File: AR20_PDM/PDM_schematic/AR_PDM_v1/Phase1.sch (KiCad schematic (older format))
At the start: 22 parts, among them Q1 BTS50025-1TAD, U1 INA233

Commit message: Added LEDs and switches.
- Added all status leds
- Added all switches
- ! Connections are work in progress, not everything is correct
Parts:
- removed D?: P1_Active, symbol Device:LED
- removed R? (x2): 4k7, symbol AR20_PDM_v1-rescue:R-Device
- removed R?: RLED, symbol AR20_PDM_v1-rescue:R-Device
- removed U? (x2): Fet-P, symbol AR20_PDM_v1-rescue:GenericFet-P
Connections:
- net labels added: P1_MOS_IN
- net labels removed: P1_Alert, P1_EN_ACM, P1_EN_AUX
- wire segments 81 -> 59
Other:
- note removed: "Use Logic Level Mosfets. (Gs Threshold <3.3V)\nP-mos array might be used"
- moved on the sheet: C_sense?

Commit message: Fixed wrong value components and ports, wiring, see discription
- Fixed supply cappacitor value 220 nf to 100nf
- Fixed IN cappacitor value 220 nf to 150 nf
- Fixed out cappacitor value, 220nf to 10 nf
- Made a mux for mosfet sense
- Found a I/O port expander
- Added some and removed some leds
- Fixed all labels, and wired everything up, besides the connectors
- Still missing connector and acm connector pinout.
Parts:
- removed C_sense?: 0.1uf, symbol AR20_PDM_v1-rescue:C-Device
- C_bypass: value 0.1uF -> 100nf
- C_in: value 220nf -> 150nf
- C_out: value 220nf -> 10nf
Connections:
- wire segments 59 -> 57
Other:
- note removed: "Ceramic, Place close to respective phase, mosfet/relay"
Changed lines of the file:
@@
 $Descr A4 11693 8268
 encoding utf-8
-Sheet 4 11
+Sheet 4 13
 Title ""
 Date ""
@@
 AR Path="/5E10174B/5DAAC1D1" Ref="C_out?"  Part="1"
 F 0 "C_out" H 4915 2896 50  0000 L CNN
-F 1 "220nf" H 4915 2805 50  0000 L CNN
+F 1 "10nf" H 4915 2805 50  0000 L CNN
 F 2 "" H 4838 2700 50  0001 C CNN
 F 3 "~" H 4800 2850 50  0001 C CNN
@@
 AR Path="/5E10174B/5DAAC1D7" Ref="C_in?"  Part="1"
 F 0 "C_in" H 3615 1996 50  0000 L CNN
-F 1 "220nf" H 3615 1905 50  0000 L CNN
+F 1 "150nf" H 3615 1905 50  0000 L CNN
 F 2 "" H 3538 1800 50  0001 C CNN
 F 3 "~" H 3500 1950 50  0001 C CNN
@@
 AR Path="/5E10174B/5DAAC201" Ref="C_bypass?"  Part="1"
 F 0 "C_bypass" V 8248 3350 50  0000 C CNN
-F 1 "0.1uF" V 8339 3350 50  0000 C CNN
+F 1 "100nf" V 8339 3350 50  0000 C CNN
 F 2 "" H 8538 3200 50  0001 C CNN
 F 3 "~" H 8500 3350 50  0001 C CNN
@@
 Wire Wire Line
 	6575 4300 8750 4300
-$Comp
-L AR20_PDM_v1-rescue:C-Device C_sense?
-U 1 1 5E10B301
-P 7225 1925
-AR Path="/5DA89415/5E10B301" Ref="C_sense?"  Part="1"
-AR Path="/5DEB10A1/5E10B301" Ref="C_sense?"  Part="1"
-AR Path="/5DEB20EA/5E10B301" Ref="C_sense?"  Part="1"
-AR Path="/5E0E4725/5E10B301" Ref="C_sense?"  Part="1"
-AR Path="/5E0E4A93/5E10B301" Ref="C_sense?"  Part="1"
-AR Path="/5E0E4EB5/5E10B301" Ref="C_sense?"  Part="1"
-AR Path="/5E0E5304/5E10B301" Ref="C_sense?"  Part="1"
-AR Path="/5E0E594B/5E10B301" Ref="C_sense?"  Part="1"
-AR Path="/5E0E607C/5E10B301" Ref="C_sense?"  Part="1"
-AR Path="/5E0FB5C8/5E10B301" Ref="C_sense?"  Part="1"
-AR Path="/5E0FBBBD/5E10B301" Ref="C_sense?"  Part="1"
-AR Path="/5E0FC3A2/5E10B301" Ref="C_sense?"  Part="1"
-AR Path="/5E0FCFDC/5E10B301" Ref="C_sense?"  Part="1"
-AR Path="/5E0FDCCC/5E10B301" Ref="C_sense?"  Part="1"
-AR Path="/5E10174B/5E10B301" Ref="C_sense?"  Part="1"
-F 0 "C_sense?" H 7340 1971 50  0000 L CNN
-F 1 "0.1uf" H 7340 1880 50  0000 L CNN
-F 2 "" H 7263 1775 50  0001 C CNN
-F 3 "~" H 7225 1925 50  0001 C CNN
-	1    7225 1925
-	-1   0    0    1
-$EndComp
-$Comp
-L AR20_PDM_v1-rescue:GND-power #PWR?
-U 1 1 5E1293CC
-P 7225 2075
-AR Path="/5DA89415/5E1293CC" Ref="#PWR?"  Part="1"
-AR Path="/5DEB10A1/5E1293CC" Ref="#PWR?"  Part="1"
-AR Path="/5DEB20EA/5E1293CC" Ref="#PWR?"  Part="1"
-AR Path="/5E0E4725/5E1293CC" Ref="#PWR?"  Part="1"
-AR Path="/5E0E4A93/5E1293CC" Ref="#PWR?"  Part="1"
-AR Path="/5E0E4EB5/5E1293CC" Ref="#PWR?"  Part="1"
-AR Path="/5E0E5304/5E1293CC" Ref="#PWR?"  Part="1"
-AR Path="/5E0E594B/5E1293CC" Ref="#PWR?"  Part="1"
-AR Path="/5E0E607C/5E1293CC" Ref="#PWR?"  Part="1"
-AR Path="/5E0FB5C8/5E1293CC" Ref="#PWR?"  Part="1"
-AR Path="/5E0FBBBD/5E1293CC" Ref="#PWR?"  Part="1"
-AR Path="/5E0FC3A2/5E1293CC" Ref="#PWR?"  Part="1"
-AR Path="/5E0FCFDC/5E1293CC" Ref="#PWR?"  Part="1"
-AR Path="/5E0FDCCC/5E1293CC" Ref="#PWR?"  Part="1"
-AR Path="/5E10174B/5E1293CC" Ref="#PWR?"  Part="1"
-F 0 "#PWR?" H 7225 1825 50  0001 C CNN
-F 1 "GND" H 7230 1902 50  0000 C CNN
-F 2 "" H 7225 2075 50  0001 C CNN
-F 3 "" H 7225 2075 50  0001 C CNN
-	1    7225 2075
-	1    0    0    -1
-$EndComp
-Wire Wire Line
-	7225 1775 7225 1675
-Wire Wire Line
-	7225 1675 7150 1675
-Text Notes 6800 2400 0    50   ~ 0
-Ceramic, Place close to respective phase, mosfet/relay
 Wire Wire Line
 	3700 3225 4525 3225
@@
 Text HLabel 4650 1600 0    50   Input ~ 10
 V+12V
-Text HLabel 7150 1675 0    50   Input ~ 10
-V+12V
-Wire Notes Line
-	6725 1600 9050 1600
-Wire Notes Line
-	9050 1600 9050 2450
-Wire Notes Line
-	9050 2450 6725 2450
-Wire Notes Line
-	6725 2450 6725 1600
 Wire Wire Line
 	2250 2400 3150 2400

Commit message: Fixed issues, controlled components, BOM, see discription
- added acm symbol
- fixed wrongly faced P-mosfets
- I/O expander now sinks led instead of source
- Bill of material mostly done
- Correct address for INA233 chips.
- Now 4 diodes serves as flyback for all mosfets
- Corrected naming scheme for compmonents (everything is not fixed yet)
- Fixed some labels
- altso some minor changes
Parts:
- removed C_bypass, C_vs: 100nf, symbol AR20_PDM_v1-rescue:C-Device
- removed C_out, C_sense: 10nf, symbol AR20_PDM_v1-rescue:C-Device
- removed Cs?: 4.7uF, symbol AR20_PDM_v1-rescue:C-Device
- removed D?: 3.3-5V 5W, symbol AR20_PDM_v1-rescue:D_Zener-Device
- removed D?: 16V 5W, symbol AR20_PDM_v1-rescue:D_Zener-Device
- removed Q1: BTS50025-1TAD, symbol AR20_PDM_v1-rescue:BTS50025-1TAD
- removed R?: 4k7, symbol AR20_PDM_v1-rescue:R-Device
- removed R_Shunt: 5m_0.1%_30+A, symbol AR20_PDM_v1-rescue:R_Shunt-Device
- removed R_in: 4.7K, symbol AR20_PDM_v1-rescue:R-Device
- removed R_s?: 3.9R, symbol AR20_PDM_v1-rescue:R-Device
- removed R_sense: 1k, symbol AR20_PDM_v1-rescue:R-Device
- removed U1: INA233, symbol AR20_PDM_v1-rescue:INA233
- added C10: 4.7uF, Capacitor_SMD:C_1206_3216Metric, symbol AR20_PDM_v1-rescue:C-Device
- added C11, C9: 100nf, Capacitor_SMD:C_0603_1608Metric, symbol AR20_PDM_v1-rescue:C-Device
- added C6, C8: 10nf, Capacitor_SMD:C_0603_1608Metric, symbol AR20_PDM_v1-rescue:C-Device
- added Q3: BTS50025-1TAD, symbol AR20_PDM_v1-rescue:BTS50025-1TAD
- added R3, R4: 4k7, symbol AR20_PDM_v1-rescue:R-Device
- added R5: 1k, symbol AR20_PDM_v1-rescue:R-Device
- added R6: 3.9R, symbol AR20_PDM_v1-rescue:R-Device
- added R_Shunt4: 2m_1%_4W, symbol AR20_PDM_v1-rescue:R-Device
- added U5: INA233, symbol AR20_PDM_v1-rescue:INA233
- C7: renamed from C_in; footprint (none) -> Capacitor_SMD:C_0603_1608Metric
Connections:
- wire segments 57 -> 55
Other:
- note added: "addr: 1000000"

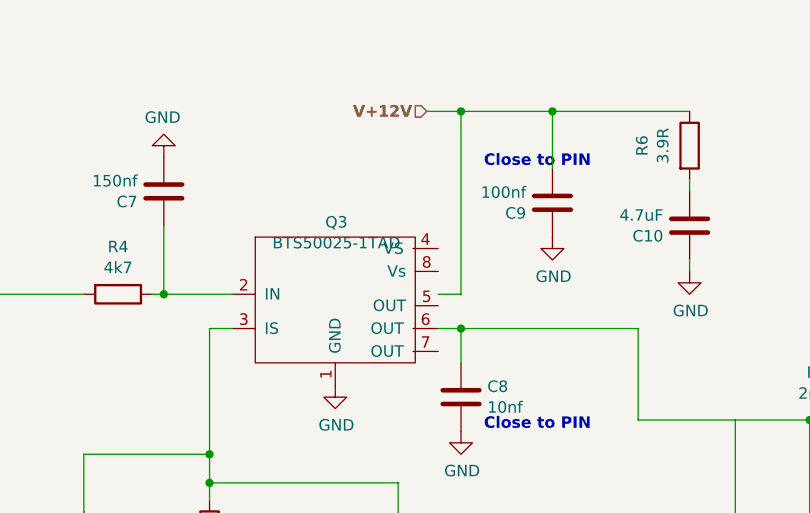
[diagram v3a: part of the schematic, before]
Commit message: PCB design, and issue fixing, work in progress
- Error fixed: Mux mosfet resistor change to ground
- Open drain output added on phase 6, for engine blipping purpose
- Most of pcb symbols and footprints are finished, including main connector
- PCB is change from 1oz to 2oz copper layer, for easier routing.
- Basic Draft of pcb is done, for now.
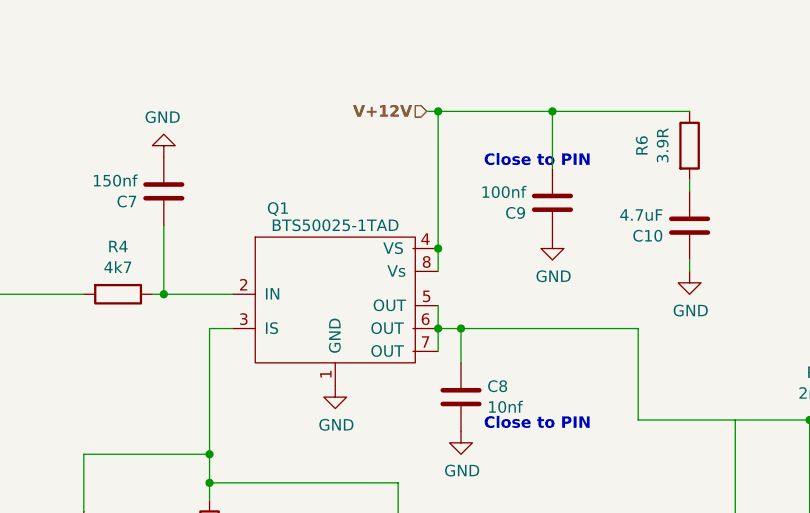
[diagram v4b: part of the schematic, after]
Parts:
- Q1: renamed from Q3; footprint (none) -> AR_PDM_v1:BTS500xx
- R3, R4, R5, R6: footprint (none) -> Resistor_SMD:R_0603_1608Metric
- R_Shunt4: footprint (none) -> Resistor_SMD:R_2512_6332Metric
- U5: footprint (none) -> AR_PDM_v1:INA233
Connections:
- net V+12V: now also Q1.4 (VS), Q1.8 (Vs)
- net at C8.1, Q1.6 (OUT), R_Shunt4.2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: now also Q1.5 (OUT), Q1.7 (OUT)
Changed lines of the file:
@@
 F 0 "R4" V 3093 2400 50  0000 C CNN
 F 1 "4k7" V 3184 2400 50  0000 C CNN
-F 2 "" V 3230 2400 50  0001 C CNN
+F 2 "Resistor_SMD:R_0603_1608Metric" V 3230 2400 50  0001 C CNN
 F 3 "~" H 3300 2400 50  0001 C CNN
 	1    3300 2400
@@
 F 0 "R3" H 2320 1896 50  0000 L CNN
 F 1 "4k7" H 2320 1805 50  0000 L CNN
-F 2 "" V 2180 1850 50  0001 C CNN
+F 2 "Resistor_SMD:R_0603_1608Metric" V 2180 1850 50  0001 C CNN
 F 3 "~" H 2250 1850 50  0001 C CNN
 	1    2250 1850
@@
 Wire Wire Line
 	3500 2100 3500 2400
-Connection ~ 3500 2400
-Wire Wire Line
-	3500 2400 3800 2400
-$Comp
-L AR20_PDM_v1-rescue:BTS50025-1TAD Q3
+$Comp
+L AR20_PDM_v1-rescue:BTS50025-1TAD Q1
 U 1 1 5E21B7FE
 P 4250 2650
-AR Path="/5DA89415/5E21B7FE" Ref="Q3"  Part="1"
+AR Path="/5DA89415/5E21B7FE" Ref="Q1"  Part="1"
 AR Path="/5DEB10A1/5E21B7FE" Ref="Q?"  Part="1"
 AR Path="/5DEB20EA/5E21B7FE" Ref="Q?"  Part="1"
@@
 AR Path="/5E0FDCCC/5E21B7FE" Ref="Q?"  Part="1"
 AR Path="/5E10174B/5E21B7FE" Ref="Q?"  Part="1"
-F 0 "Q3" H 4255 3215 50  0000 C CNN
-F 1 "BTS50025-1TAD" H 4255 3124 50  0000 C CNN
-F 2 "" H 4250 2650 50  0001 C CNN
+F 0 "Q1" H 4000 3275 50  0000 C CNN
+F 1 "BTS50025-1TAD" H 4250 3200 50  0000 C CNN
+F 2 "AR_PDM_v1:BTS500xx" H 4250 2650 50  0001 C CNN
 F 3 "" H 4250 2650 50  0001 C CNN
 	1    4250 2650
@@
 F 0 "U5" H 9225 4465 50  0000 C CNN
 F 1 "INA233" H 9225 4374 50  0000 C CNN
-F 2 "" H 9200 4050 50  0001 C CNN
+F 2 "AR_PDM_v1:INA233" H 9200 4050 50  0001 C CNN
 F 3 "" H 9200 4050 50  0001 C CNN
 	1    9200 4050
@@
 Wire Wire Line
 	3700 3100 3700 3225
-Wire Wire Line
-	4700 2400 4800 2400
-Wire Wire Line
-	4800 2400 4800 1600
-Wire Wire Line
-	4800 1600 4650 1600
 Text HLabel 2250 1550 1    50   Input ~ 10
 vcc_5v
@@
 F 0 "R6" V 5593 1750 50  0000 C CNN
 F 1 "3.9R" V 5684 1750 50  0000 C CNN
-F 2 "" V 5730 1750 50  0001 C CNN
+F 2 "Resistor_SMD:R_0603_1608Metric" V 5730 1750 50  0001 C CNN
 F 3 "~" H 5800 1750 50  0001 C CNN
 	1    5800 1750
@@
 Wire Wire Line
 	5200 1600 5800 1600
-Wire Wire Line
-	4800 1600 5200 1600
-Connection ~ 4800 1600
 Connection ~ 5200 1600
 Text HLabel 1350 1900 1    50   Input ~ 10
@@
 F 0 "R5" H 3770 3496 50  0000 L CNN
 F 1 "1k" H 3770 3405 50  0000 L CNN
-F 2 "" V 3630 3450 50  0001 C CNN
+F 2 "Resistor_SMD:R_0603_1608Metric" V 3630 3450 50  0001 C CNN
 F 3 "~" H 3700 3450 50  0001 C CNN
 	1    3700 3450
@@
 F 0 "R_Shunt4" V 6268 2950 50  0000 C CNN
 F 1 "2m_1%_4W" V 6359 2950 50  0000 C CNN
-F 2 "" V 6405 2950 50  0001 C CNN
+F 2 "Resistor_SMD:R_2512_6332Metric" V 6405 2950 50  0001 C CNN
 F 3 "~" H 6475 2950 50  0001 C CNN
 	1    6475 2950
@@
 Text Notes 10125 4800 0    50   ~ 0
 addr: 1000000
+Wire Wire Line
+	4650 1600 4700 1600
+Wire Wire Line
+	4700 2200 4700 2300
+Wire Wire Line
+	4700 2200 4700 1600
+Connection ~ 4700 2200
+Connection ~ 4700 1600
+Wire Wire Line
+	4700 1600 5200 1600
+Wire Wire Line
+	4700 2450 4700 2550
+Connection ~ 4700 2550
+Wire Wire Line
+	4700 2550 4700 2650
+Connection ~ 3500 2400
+Wire Wire Line
+	3500 2400 3800 2400
 $EndSCHEMATC

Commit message: PCB Design, Work in progress
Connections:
- net P1_Shunt: now reaches C8.1, Q1.5 (OUT), Q1.6 (OUT), Q1.7 (OUT), R_Shunt4.2, U5.8 (VBUS), U5.9 (In-)
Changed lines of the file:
@@
 $Descr A4 11693 8268
 encoding utf-8
-Sheet 4 13
+Sheet 3 13
 Title ""
 Date ""
@@
 Wire Wire Line
 	6325 2950 6325 4400
-Wire Wire Line
-	6000 2950 6325 2950
 $Comp
 L AR20_PDM_v1-rescue:R-Device R_Shunt4
@@
 Wire Wire Line
 	3500 2400 3800 2400
+Wire Wire Line
+	6000 2950 6000 2825
+Text HLabel 6000 2825 1    50   Input ~ 0
+P1_Shunt
+Connection ~ 6000 2950
+Wire Wire Line
+	6000 2950 6325 2950
 $EndSCHEMATC

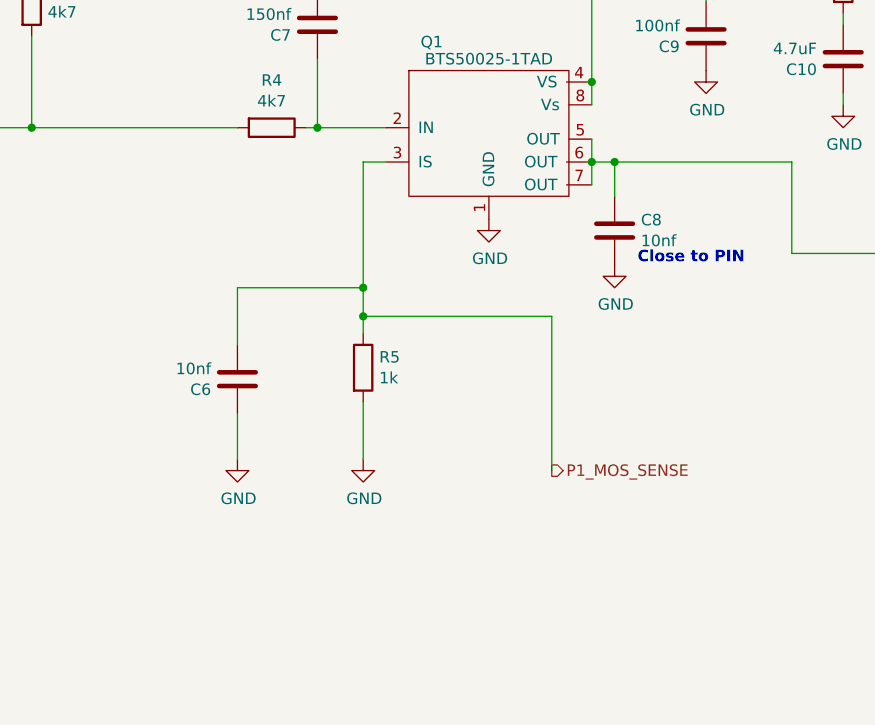
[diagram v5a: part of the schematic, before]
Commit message: PCB Design,  minor schematics changes, work in progress, see description
- Removed mos sense caps and resistors accept one, 
since only one measurement can be done, at a time.
- added mos sens protection resistors on each line, to protect mux mosfets and micro controller. 
- Routing plan mostly finalized, some of the traces are just proof of concept.
those needs to be routed nicely.
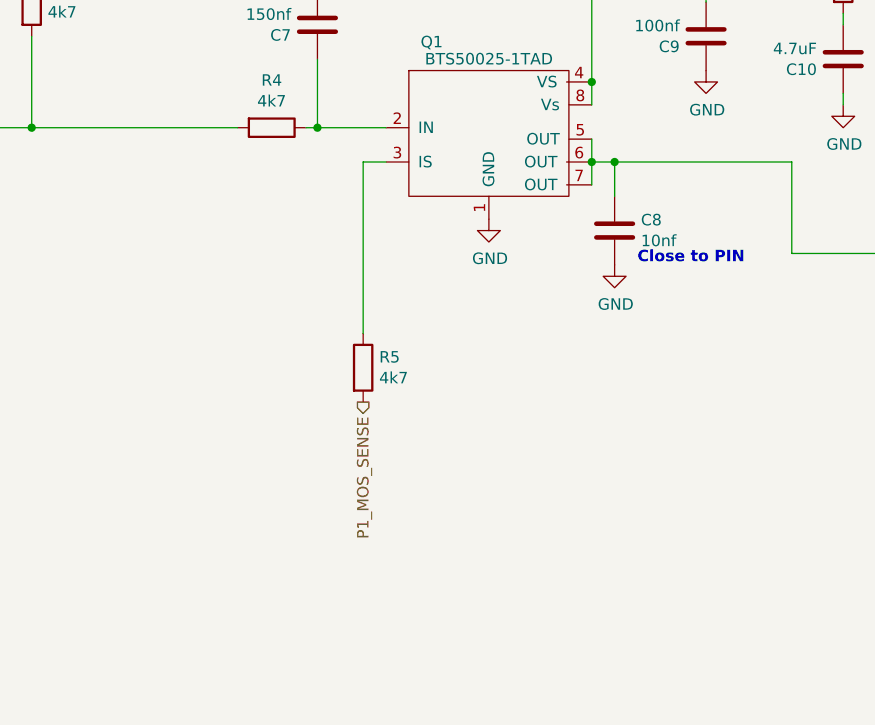
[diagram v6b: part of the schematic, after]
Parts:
- removed C6: 10nf, Capacitor_SMD:C_0603_1608Metric, symbol AR20_PDM_v1-rescue:C-Device
- R5: value 1k -> 4k7
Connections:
- net GND: no longer R5.2
- net P1_MOS_SENSE: now also R5.2; no longer Q1.3 (IS), R5.1
- new net: Q1.3 (IS), R5.1
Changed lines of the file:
@@
-$EndComp
-$Comp
-L AR20_PDM_v1-rescue:GND-power #PWR028
-U 1 1 5E21B823
-P 3700 3850
-AR Path="/5DA89415/5E21B823" Ref="#PWR028"  Part="1"
-AR Path="/5DEB10A1/5E21B823" Ref="#PWR?"  Part="1"
-AR Path="/5DEB20EA/5E21B823" Ref="#PWR?"  Part="1"
-AR Path="/5E0E4725/5E21B823" Ref="#PWR?"  Part="1"
-AR Path="/5E0E4A93/5E21B823" Ref="#PWR?"  Part="1"
-AR Path="/5E0E4EB5/5E21B823" Ref="#PWR?"  Part="1"
-AR Path="/5E0E5304/5E21B823" Ref="#PWR?"  Part="1"
-AR Path="/5E0E594B/5E21B823" Ref="#PWR?"  Part="1"
-AR Path="/5E0E607C/5E21B823" Ref="#PWR?"  Part="1"
-AR Path="/5E0FB5C8/5E21B823" Ref="#PWR?"  Part="1"
-AR Path="/5E0FBBBD/5E21B823" Ref="#PWR?"  Part="1"
-AR Path="/5E0FC3A2/5E21B823" Ref="#PWR?"  Part="1"
-AR Path="/5E0FCFDC/5E21B823" Ref="#PWR?"  Part="1"
-AR Path="/5E0FDCCC/5E21B823" Ref="#PWR?"  Part="1"
-AR Path="/5E10174B/5E21B823" Ref="#PWR?"  Part="1"
-F 0 "#PWR028" H 3700 3600 50  0001 C CNN
-F 1 "GND" H 3705 3677 50  0000 C CNN
-F 2 "" H 3700 3850 50  0001 C CNN
-F 3 "" H 3700 3850 50  0001 C CNN
-	1    3700 3850
-	1    0    0    -1
 $EndComp
 $Comp
@@
 $EndComp
 Wire Wire Line
-	3700 2550 3700 3100
-Wire Wire Line
 	3700 2550 3800 2550
-Wire Wire Line
-	3700 3850 3700 3600
 Wire Wire Line
 	8750 2850 8750 3350
@@
 Wire Wire Line
 	9700 4450 10000 4450
-$Comp
-L AR20_PDM_v1-rescue:GND-power #PWR026
-U 1 1 5E21B848
-P 3150 3850
-AR Path="/5DA89415/5E21B848" Ref="#PWR026"  Part="1"
-AR Path="/5DEB10A1/5E21B848" Ref="#PWR?"  Part="1"
-AR Path="/5DEB20EA/5E21B848" Ref="#PWR?"  Part="1"
-AR Path="/5E0E4725/5E21B848" Ref="#PWR?"  Part="1"
-AR Path="/5E0E4A93/5E21B848" Ref="#PWR?"  Part="1"
-AR Path="/5E0E4EB5/5E21B848" Ref="#PWR?"  Part="1"
-AR Path="/5E0E5304/5E21B848" Ref="#PWR?"  Part="1"
-AR Path="/5E0E594B/5E21B848" Ref="#PWR?"  Part="1"
-AR Path="/5E0E607C/5E21B848" Ref="#PWR?"  Part="1"
-AR Path="/5E0FB5C8/5E21B848" Ref="#PWR?"  Part="1"
-AR Path="/5E0FBBBD/5E21B848" Ref="#PWR?"  Part="1"
-AR Path="/5E0FC3A2/5E21B848" Ref="#PWR?"  Part="1"
-AR Path="/5E0FCFDC/5E21B848" Ref="#PWR?"  Part="1"
-AR Path="/5E0FDCCC/5E21B848" Ref="#PWR?"  Part="1"
-AR Path="/5E10174B/5E21B848" Ref="#PWR?"  Part="1"
-F 0 "#PWR026" H 3150 3600 50  0001 C CNN
-F 1 "GND" H 3155 3677 50  0000 C CNN
-F 2 "" H 3150 3850 50  0001 C CNN
-F 3 "" H 3150 3850 50  0001 C CNN
-	1    3150 3850
-	1    0    0    -1
-$EndComp
-$Comp
-L AR20_PDM_v1-rescue:C-Device C6
-U 1 1 5E21B851
-P 3150 3500
-AR Path="/5DA89415/5E21B851" Ref="C6"  Part="1"
-AR Path="/5DEB10A1/5E21B851" Ref="C?"  Part="1"
-AR Path="/5DEB20EA/5E21B851" Ref="C?"  Part="1"
-AR Path="/5E0E4725/5E21B851" Ref="C?"  Part="1"
-AR Path="/5E0E4A93/5E21B851" Ref="C?"  Part="1"
-AR Path="/5E0E4EB5/5E21B851" Ref="C?"  Part="1"
-AR Path="/5E0E5304/5E21B851" Ref="C?"  Part="1"
-AR Path="/5E0E594B/5E21B851" Ref="C?"  Part="1"
-AR Path="/5E0E607C/5E21B851" Ref="C?"  Part="1"
-AR Path="/5E0FB5C8/5E21B851" Ref="C?"  Part="1"
-AR Path="/5E0FBBBD/5E21B851" Ref="C?"  Part="1"
-AR Path="/5E0FC3A2/5E21B851" Ref="C?"  Part="1"
-AR Path="/5E0FCFDC/5E21B851" Ref="C?"  Part="1"
-AR Path="/5E0FDCCC/5E21B851" Ref="C?"  Part="1"
-AR Path="/5E10174B/5E21B851" Ref="C?"  Part="1"
-F 0 "C6" H 3265 3546 50  0000 L CNN
-F 1 "10nf" H 3265 3455 50  0000 L CNN
-F 2 "Capacitor_SMD:C_0603_1608Metric" H 3188 3350 50  0001 C CNN
-F 3 "~" H 3150 3500 50  0001 C CNN
-	1    3150 3500
-	-1   0    0    1
-$EndComp
 Wire Wire Line
 	3450 2400 3500 2400
@@
 Text Notes 8200 3050 0    50   ~ 10
 Close to PIN
-Wire Wire Line
-	3150 3100 3150 3350
-Wire Wire Line
-	3150 3650 3150 3850
-Wire Wire Line
-	3150 3100 3700 3100
-Connection ~ 3700 3100
-Wire Wire Line
-	3700 3100 3700 3225
 Text HLabel 2250 1550 1    50   Input ~ 10
 vcc_5v
@@
 AR Path="/5E10174B/5E21B875" Ref="R?"  Part="1"
 F 0 "R5" H 3770 3496 50  0000 L CNN
-F 1 "1k" H 3770 3405 50  0000 L CNN
+F 1 "4k7" H 3770 3405 50  0000 L CNN
 F 2 "Resistor_SMD:R_0603_1608Metric" V 3630 3450 50  0001 C CNN
 F 3 "~" H 3700 3450 50  0001 C CNN
@@
 Wire Wire Line
 	6625 4300 8750 4300
-Wire Wire Line
-	3700 3225 4525 3225
-Wire Wire Line
-	4525 3225 4525 3900
-Connection ~ 3700 3225
-Wire Wire Line
-	3700 3225 3700 3300
-Text HLabel 4525 3900 2    50   Output ~ 0
+Text HLabel 3700 3600 3    50   Output ~ 0
 P1_MOS_SENSE
 Wire Wire Line
@@
 Wire Wire Line
 	6000 2950 6325 2950
+Wire Wire Line
+	3700 2550 3700 3300
 $EndSCHEMATC

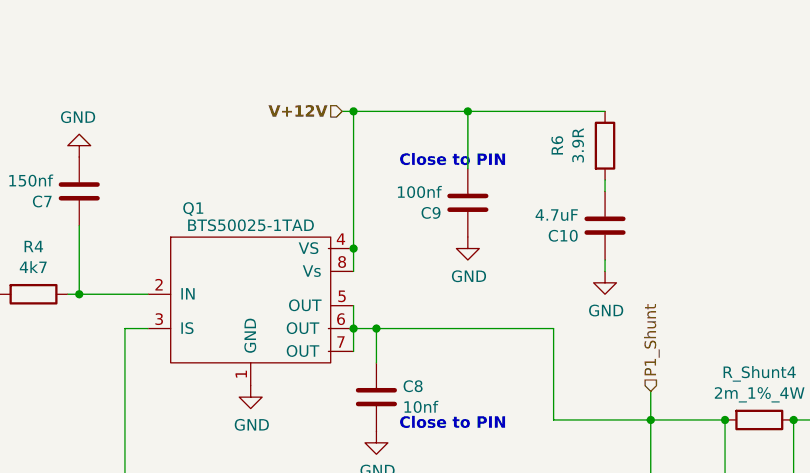
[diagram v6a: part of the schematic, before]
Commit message: First Complete Draft of PCB and schematics, - minus see discription
- missing correct smd switch header
- missing correct main power plug
- tweeks still needs to be done
- Extra inspection of schematics pending
- proper, in depth quiality controll of pcb work pending
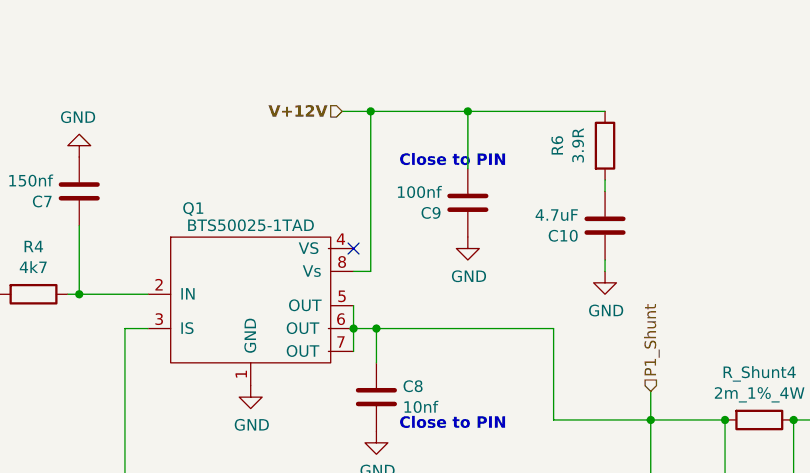
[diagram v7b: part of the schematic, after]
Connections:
- net V+12V: no longer Q1.4 (VS)
- no-connect marks 0 -> 1
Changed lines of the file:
@@
 $Descr A4 11693 8268
 encoding utf-8
-Sheet 3 13
+Sheet 2 13
 Title ""
 Date ""
@@
 addr: 1000000
 Wire Wire Line
-	4650 1600 4700 1600
-Wire Wire Line
-	4700 2200 4700 2300
-Wire Wire Line
-	4700 2200 4700 1600
-Connection ~ 4700 2200
-Connection ~ 4700 1600
-Wire Wire Line
-	4700 1600 5200 1600
-Wire Wire Line
 	4700 2450 4700 2550
 Connection ~ 4700 2550
@@
 Wire Wire Line
 	3700 2550 3700 3300
+Connection ~ 4775 1600
+Wire Wire Line
+	4775 1600 5200 1600
+Wire Wire Line
+	4650 1600 4775 1600
+Wire Wire Line
+	4775 2300 4700 2300
+Wire Wire Line
+	4775 1600 4775 2300
+NoConn ~ 4700 2200
 $EndSCHEMATC
